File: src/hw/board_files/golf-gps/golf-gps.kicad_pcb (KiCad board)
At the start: 4 copper layers, 60.4 x 88.2 mm, 68 parts, among them J1 Conn_01x04_Pin, J2 Micro_SD_Card, P1 USB_C_Plug_USB2.0, SW1 SW_SPDT, SW2 RESET, SW3 BOOT, SW4 BTN_1, SW5 BTN_2, SW6 BTN_3, U1 MCP73831-2-OT, U2 TPS63031DSKR, U3 STM32L432KCU6, U4 NEO-M9N, Y1 32.768kHz

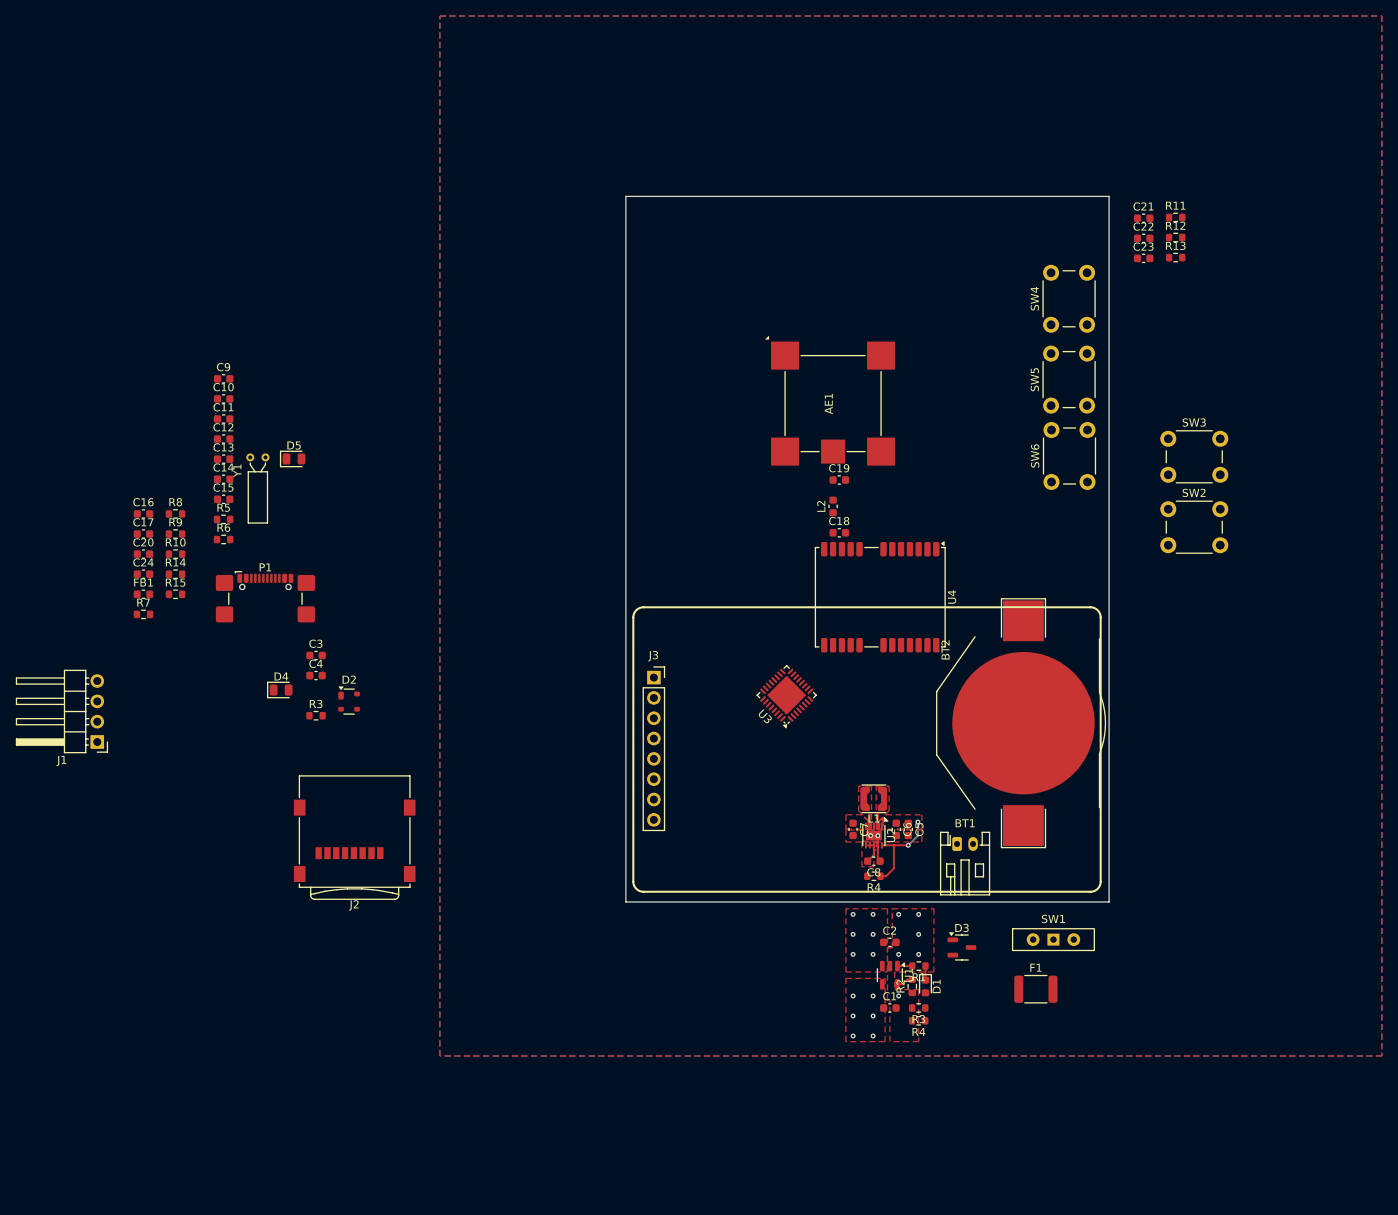
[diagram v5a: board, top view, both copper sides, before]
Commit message: Updated pinout and spreadsheet, PCB changes
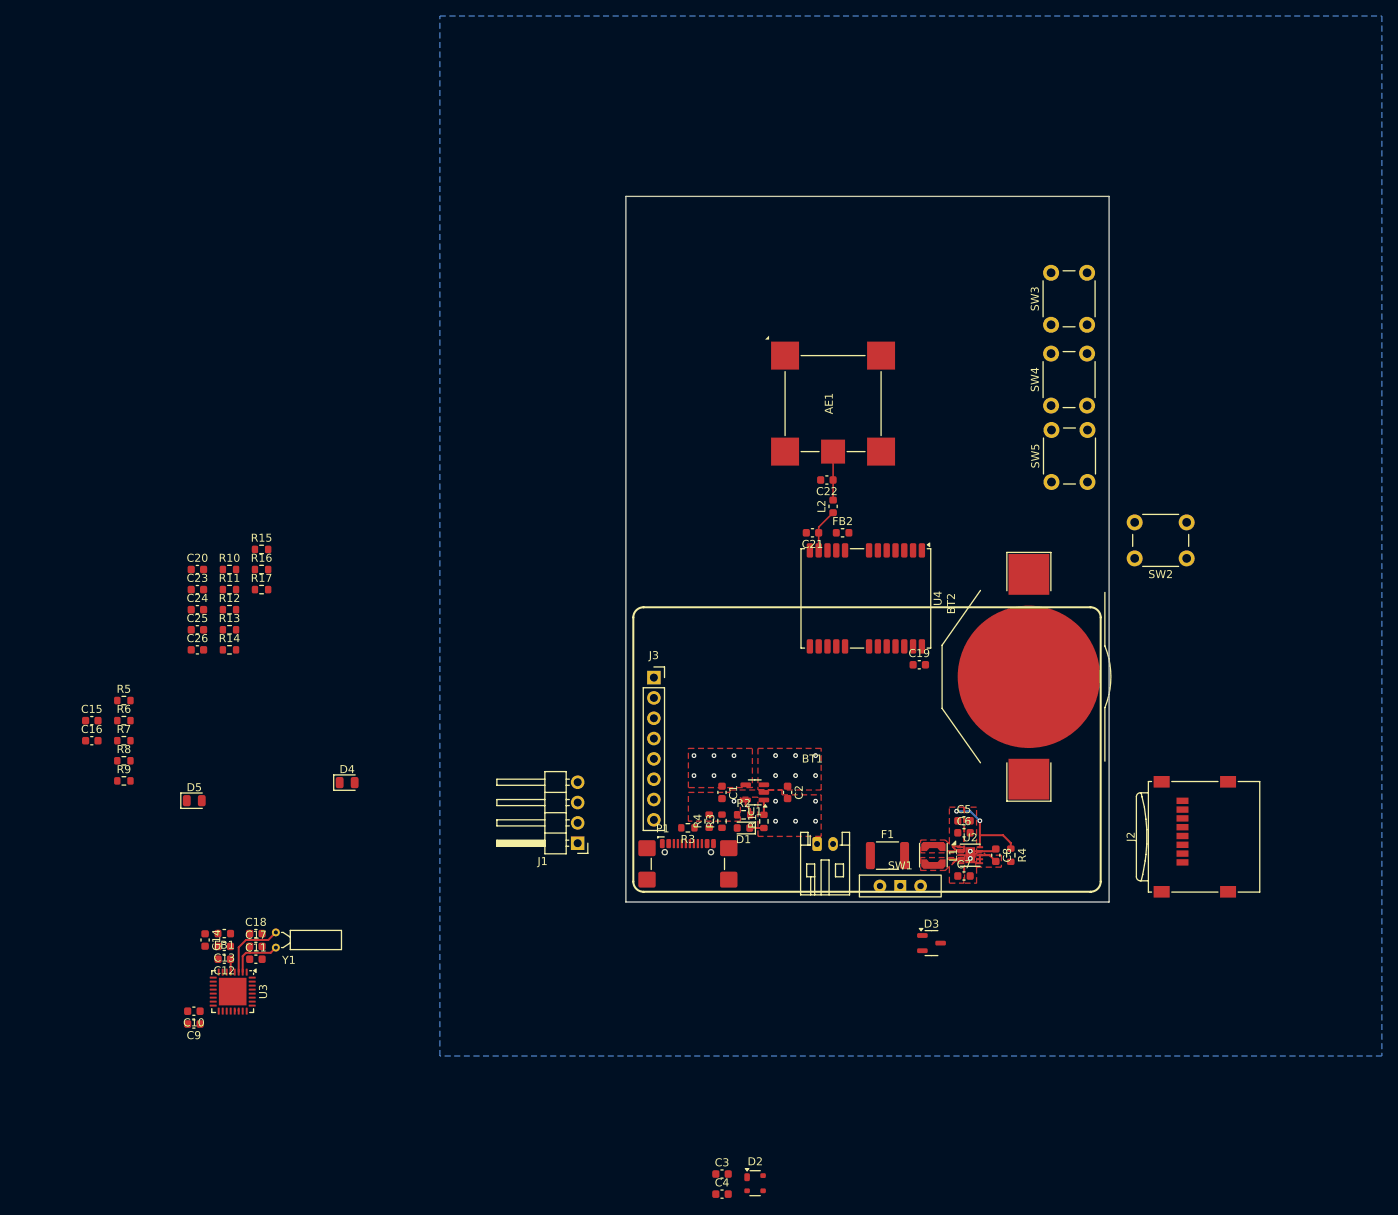
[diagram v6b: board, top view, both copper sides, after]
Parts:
- removed the C21 at (174.6, 69.2)
- removed the C22 at (174.6, 71.7)
- removed the SW3 at (177.7, 96.8)
- added C18: TBD, Capacitor_SMD:C_0603_1608Metric, F.Cu at (63.6, 158.6)
- added C19: 100n, Capacitor_SMD:C_0603_1608Metric, F.Cu at (146.6, 125.0)
- added C25: 100n, Capacitor_SMD:C_0603_1608Metric, F.Cu at (56.3, 120.6)
- added C26: 100n, Capacitor_SMD:C_0603_1608Metric, F.Cu at (56.3, 123.1)
- added FB2: TBD, Inductor_SMD:L_0603_1608Metric, F.Cu at (137.0, 108.5)
- added R16: 10k, Resistor_SMD:R_0603_1608Metric, F.Cu at (64.4, 113.1)
- added R17: 10k, Resistor_SMD:R_0603_1608Metric, F.Cu at (64.4, 115.6)
- C13: value 100n -> 2u2
- C14: value TBD -> 2u2
- C15: value TBD -> 100n
- C17: value 100n -> TBD
- D1: value LED -> LED_STAT
- R6: value 330R -> 100k
- R7: value 10k -> 100k
- R9: value 10k -> 330R
- SW2: value RESET -> BOOT
- moved R11 127.1 mm to (60.4, 115.6)
- moved R12 127.1 mm to (60.4, 118.1)
- moved R13 127.1 mm to (60.4, 120.6)
- moved C23 125.3 mm to (56.3, 115.6)
- moved J2 105.0 mm to (181.0, 146.5), turned to 90 degrees
- moved C3 82.3 mm to (121.9, 188.7)
- moved C4 82.3 mm to (121.9, 191.2)
- moved C9 80.7 mm to (55.9, 169.9), turned to 180 degrees
- moved D2 78.7 mm to (126.0, 189.8)
- moved U3 78.5 mm to (60.8, 165.8), turned to -90 degrees
- moved C10 76.6 mm to (55.9, 168.3), turned to 180 degrees
- moved C11 67.6 mm to (63.6, 161.8)
- moved C12 65.0 mm to (59.7, 161.8), turned to 180 degrees
- moved P1 62.4 mm to (117.7, 151.0)
- moved J1 61.4 mm to (103.9, 147.3)
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- renumbered C18 to C21, C19 to C22, SW4 to SW3, SW5 to SW4, SW6 to SW5
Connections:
- C12 pad 1: +3V3 -> VDDA
- C13 pad 1: GND -> VDDA
- C13 pad 2: /Microcontroller/NRST -> GND
- C14 pad 1: /Microcontroller/OSC32_IN -> +3V3
- C15 pad 1: /Microcontroller/OSC32_OUT -> /Microcontroller/NRST
- C16 pad 1: +3V3 -> /Microcontroller/BOOT0
- C16 pad 2: GND -> +3V3
- C17 pad 1: +3V3 -> /Microcontroller/OSC32_IN
- C20 pad 1: /Microcontroller/BOOT0 -> +3V3
- C20 pad 2: +3V3 -> GND
- C23 pad 2: /Microcontroller/BTN_3 -> /Microcontroller/BTN_1
- C24 pad 1: +3V3 -> GND
- C24 pad 2: GND -> /Microcontroller/BTN_2
- FB1 pad 1: Net-(U4-VCC_RF) -> VDDA
- R10 pad 1: Net-(U4-~{RESET}) -> +3V3
- R10 pad 2: +3V3 -> /Microcontroller/SD_CS
- R11 pad 1: /Microcontroller/BTN_1 -> +3V3
- R11 pad 2: +3V3 -> /Microcontroller/SPI3_MOSI
- R12 pad 1: /Microcontroller/BTN_2 -> +3V3
- R12 pad 2: +3V3 -> /Microcontroller/SPI3_MISO
- R13 pad 1: /Microcontroller/BTN_3 -> Net-(U4-~{RESET})
- R14 pad 1: /Microcontroller/BOOT0 -> /Microcontroller/BTN_1
- R14 pad 2: GND -> +3V3
- R15 pad 1: +3V3 -> /Microcontroller/BTN_2
- R15 pad 2: Net-(J3-BL) -> +3V3
- R5 pad 1: +3V3 -> /Microcontroller/NRST
- R5 pad 2: /Microcontroller/NRST -> +3V3
- R6 pad 1: /Microcontroller/LED_STATUS -> /Microcontroller/ADC1
- R6 pad 2: Net-(D5-A) -> VBAT
- R7 pad 1: +3V3 -> GND
- R7 pad 2: /Microcontroller/SD_CS -> /Microcontroller/ADC1
- R8 pad 1: +3V3 -> /Microcontroller/BOOT0
- R8 pad 2: /Microcontroller/SPI3_MOSI -> GND
- R9 pad 1: +3V3 -> /Microcontroller/LED_STATUS
- R9 pad 2: /Microcontroller/SPI3_MISO -> Net-(D5-A)
- SW2 pad 1: /Microcontroller/NRST -> /Microcontroller/BOOT0
- SW2 pad 2: GND -> +3V3
- U3 pad 5: +3V3 -> VDDA
- U3 pad 6: unconnected-(U3-PA0-Pad6) -> /Microcontroller/ADC1
- Y1 pad 1: /Microcontroller/OSC32_OUT -> /Microcontroller/OSC32_IN
- Y1 pad 2: /Microcontroller/OSC32_IN -> /Microcontroller/OSC32_OUT
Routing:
- net /Microcontroller/OSC32_OUT: track 0.00 -> 9.33 mm
- net /Microcontroller/OSC32_IN: track 0.00 -> 7.40 mm
- net Net-(AE1-A): track 0.00 -> 6.06 mm
- net Net-(U4-RF_IN): track 0.00 -> 5.46 mm
- net VDDA: track 0.00 -> 1.62 mm

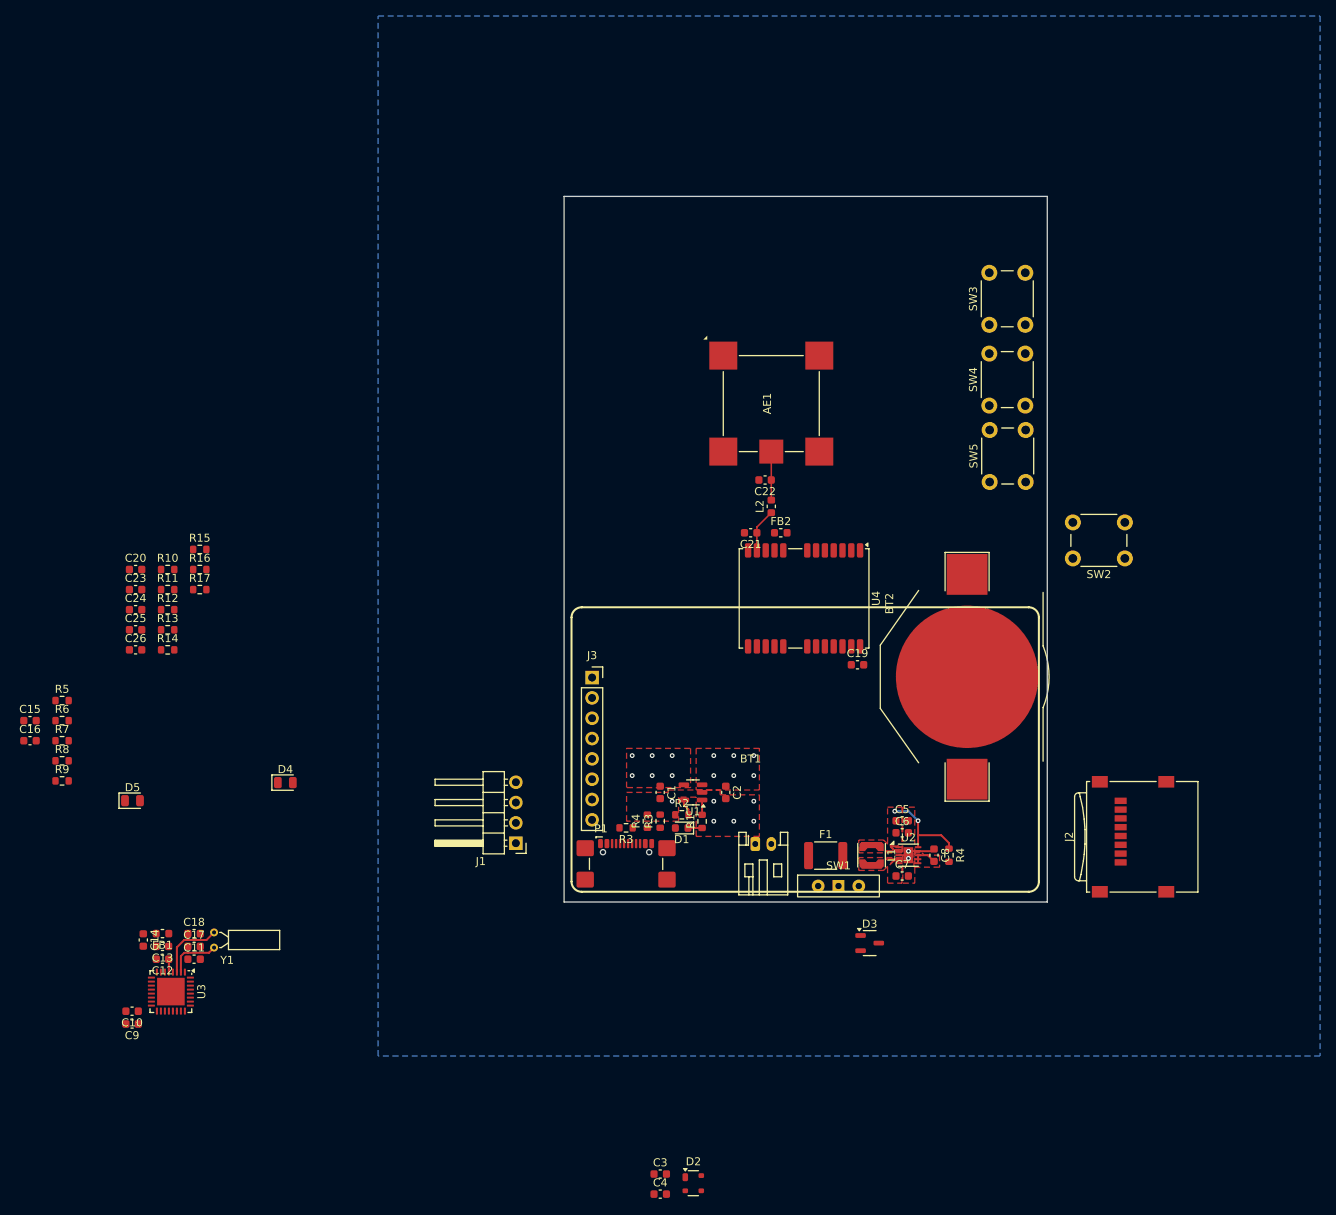
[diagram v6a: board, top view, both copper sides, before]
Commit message: Figured out general component placement and made progress routing. Removed pullup resistor from MOSI, MISO, and SCK lines
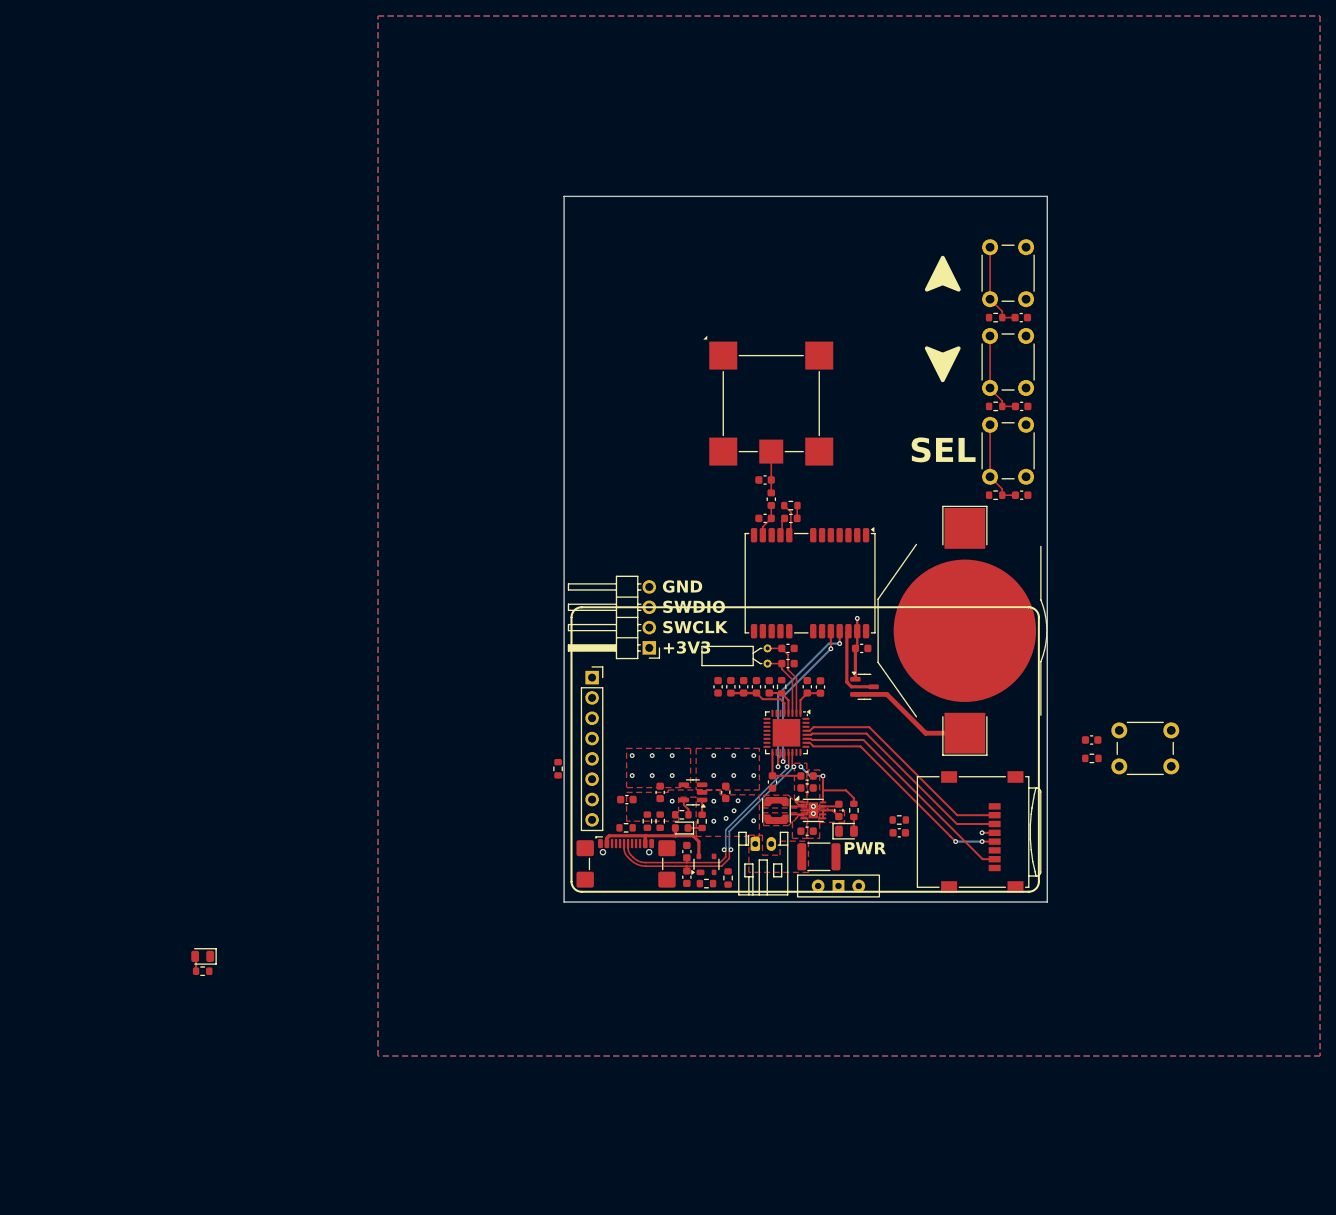
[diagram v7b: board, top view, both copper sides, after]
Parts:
- removed R11, R12: 10k, Resistor_SMD:R_0603_1608Metric
- moved C16 132.7 mm to (175.8, 134.4)
- moved R8 128.7 mm to (175.9, 136.7)
- moved C23 115.8 mm to (167.1, 81.6), turned to 180 degrees
- moved C24 113.6 mm to (167.1, 92.7), turned to 180 degrees
- moved C25 112.0 mm to (167.1, 103.8), turned to 180 degrees
- moved R14 111.5 mm to (163.8, 81.6), turned to 180 degrees
- moved R15 101.1 mm to (163.8, 92.7), turned to 180 degrees
- moved C20 101.0 mm to (151.8, 146.0), turned to 180 degrees
- moved R16 99.9 mm to (163.8, 103.8), turned to 180 degrees
- moved R10 96.7 mm to (151.8, 144.4)
- moved C9 95.8 mm to (141.9, 127.8), turned to 90 degrees
- moved C10 93.6 mm to (140.3, 127.8), turned to 90 degrees
- moved C15 92.5 mm to (135.6, 127.8), turned to 90 degrees
- moved R5 90.0 mm to (137.1, 127.8), turned to 90 degrees
- moved R6 85.5 mm to (130.4, 151.7), turned to 90 degrees
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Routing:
- net /Microcontroller/USB_D+: track 0.20 -> 32.7 mm, vias 0 -> 2
- net /Microcontroller/USB_D-: track 0.20 -> 31.1 mm, vias 0 -> 2
- net /Microcontroller/SPI3_MISO: track 0.00 -> 29.8 mm
- net /Microcontroller/SPI3_SCK: track 0.00 -> 28.7 mm, vias 0 -> 2
- net /Microcontroller/SPI3_MOSI: track 0.00 -> 28.3 mm
- net /Microcontroller/SD_CS: track 0.00 -> 28.3 mm
- net /Microcontroller/GPS_RX: track 0.00 -> 22.9 mm, vias 0 -> 2
- net +3V3: track 12.8 -> 34.6 mm, vias 2 -> 4
- net /Microcontroller/GPS_TX: track 0.00 -> 20.0 mm, vias 0 -> 2
- net V_USB: track 0.00 -> 16.4 mm
- net Net-(BT2-+): track 0.00 -> 15.7 mm
- net /Microcontroller/BTN_3: track 0.00 -> 11.1 mm
- net /Microcontroller/BTN_2: track 0.00 -> 11.1 mm
- net /Microcontroller/BTN_1: track 0.00 -> 11.0 mm
- net V_BCKP: track 0.00 -> 10.0 mm
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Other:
- board text added: "+3V3"
- board text added: "GND"
- board text added: "PWR"
- board text added: "SEL"
- board text added: "SWCLK"
- board text added: "SWDIO"
